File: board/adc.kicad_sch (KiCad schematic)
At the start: 17 parts

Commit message: ERC run
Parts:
- gave numbers to parts that had none: 17
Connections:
- net MCLK: now reaches TP18.1, U4.18 (MCLKIN)
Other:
- moved on the sheet: R17

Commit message: added footprints to symbols and started layout
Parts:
- C22, C23, C24, C25: footprint (none) -> Capacitor_SMD:C_0402_1005Metric
- J10, J11, J12, J13, J14, J7, J8, J9: footprint (none) -> Connector_PinHeader_2.54mm:PinHeader_1x03_P2.54mm_Vertical
- J6: footprint (none) -> Connector_PinHeader_2.54mm:PinHeader_1x02_P2.54mm_Vertical
- R17, R18: footprint (none) -> Resistor_SMD:R_0402_1005Metric
- TP18: footprint (none) -> TestPoint:TestPoint_Pad_D1.0mm
- U4: footprint (none) -> Package_SO:HTSSOP-20-1EP_4.4x6.5mm_P0.65mm_EP3.4x6.5mm_Mask2.75x3.43mm
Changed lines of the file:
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@@
     (property "Reference" "U4" (id 0) (at 120.65 58.42 0))
     (property "Value" "MCP3564RT" (id 1) (at 120.65 60.96 0))
-    (property "Footprint" "" (id 2) (at 109.22 69.85 0)
+    (property "Footprint" "Package_SO:HTSSOP-20-1EP_4.4x6.5mm_P0.65mm_EP3.4x6.5mm_Mask2.75x3.43mm" (id 2) (at 109.22 69.85 0)
       (effects (font (size 1.27 1.27)) hide)
     )
@@
       (effects (font (size 1.27 1.27)) (justify left))
     )
-    (property "Footprint" "" (id 2) (at 99.06 83.82 0)
+    (property "Footprint" "Capacitor_SMD:C_0402_1005Metric" (id 2) (at 99.06 83.82 0)
       (effects (font (size 1.27 1.27)) hide)
     )
@@
       (effects (font (size 1.27 1.27)) (justify left))
     )
-    (property "Footprint" "" (id 2) (at 198.12 25.4 0)
+    (property "Footprint" "Connector_PinHeader_2.54mm:PinHeader_1x03_P2.54mm_Vertical" (id 2) (at 198.12 25.4 0)
       (effects (font (size 1.27 1.27)) hide)
     )
@@
       (effects (font (size 1.27 1.27)) (justify left))
     )
-    (property "Footprint" "" (id 2) (at 86.36 83.82 0)
+    (property "Footprint" "Capacitor_SMD:C_0402_1005Metric" (id 2) (at 86.36 83.82 0)
       (effects (font (size 1.27 1.27)) hide)
     )
@@
       (effects (font (size 1.27 1.27)) (justify left))
     )
-    (property "Footprint" "" (id 2) (at 198.12 152.4 0)
+    (property "Footprint" "Connector_PinHeader_2.54mm:PinHeader_1x03_P2.54mm_Vertical" (id 2) (at 198.12 152.4 0)
       (effects (font (size 1.27 1.27)) hide)
     )
@@
       (effects (font (size 1.27 1.27)) (justify left))
     )
-    (property "Footprint" "" (id 2) (at 198.12 76.2 0)
+    (property "Footprint" "Connector_PinHeader_2.54mm:PinHeader_1x03_P2.54mm_Vertical" (id 2) (at 198.12 76.2 0)
       (effects (font (size 1.27 1.27)) hide)
     )
@@
       (effects (font (size 1.27 1.27)) (justify left))
     )
-    (property "Footprint" "" (id 2) (at 99.06 68.58 0)
+    (property "Footprint" "Capacitor_SMD:C_0402_1005Metric" (id 2) (at 99.06 68.58 0)
       (effects (font (size 1.27 1.27)) hide)
     )
@@
       (effects (font (size 1.27 1.27)) (justify left))
     )
-    (property "Footprint" "" (id 2) (at 198.12 101.6 0)
+    (property "Footprint" "Connector_PinHeader_2.54mm:PinHeader_1x03_P2.54mm_Vertical" (id 2) (at 198.12 101.6 0)
       (effects (font (size 1.27 1.27)) hide)
     )
@@
     (property "Reference" "J6" (id 0) (at 97.79 77.47 0))
     (property "Value" "REF" (id 1) (at 97.79 74.93 0))
-    (property "Footprint" "" (id 2) (at 104.14 77.47 0)
+    (property "Footprint" "Connector_PinHeader_2.54mm:PinHeader_1x02_P2.54mm_Vertical" (id 2) (at 104.14 77.47 0)
       (effects (font (size 1.27 1.27)) hide)
     )
@@
     (property "Reference" "R17" (id 0) (at 69.85 73.66 90))
     (property "Value" "10R" (id 1) (at 69.85 76.2 90))
-    (property "Footprint" "" (id 2) (at 69.85 80.01 0)
+    (property "Footprint" "Resistor_SMD:R_0402_1005Metric" (id 2) (at 69.85 80.01 0)
       (effects (font (size 1.27 1.27)) hide)
     )
@@
       (effects (font (size 1.27 1.27)) (justify left))
     )
-    (property "Footprint" "" (id 2) (at 86.36 68.58 0)
+    (property "Footprint" "Capacitor_SMD:C_0402_1005Metric" (id 2) (at 86.36 68.58 0)
       (effects (font (size 1.27 1.27)) hide)
     )
@@
       (effects (font (size 1.27 1.27)) (justify left))
     )
-    (property "Footprint" "" (id 2) (at 86.36 60.96 0)
+    (property "Footprint" "Resistor_SMD:R_0402_1005Metric" (id 2) (at 86.36 60.96 0)
       (effects (font (size 1.27 1.27)) hide)
     )
@@
       (effects (font (size 1.27 1.27)) (justify right))
     )
-    (property "Footprint" "" (id 2) (at 86.36 97.79 0)
+    (property "Footprint" "TestPoint:TestPoint_Pad_D1.0mm" (id 2) (at 86.36 97.79 0)
       (effects (font (size 1.27 1.27)) hide)
     )
@@
       (effects (font (size 1.27 1.27)) (justify left))
     )
-    (property "Footprint" "" (id 2) (at 198.12 50.8 0)
+    (property "Footprint" "Connector_PinHeader_2.54mm:PinHeader_1x03_P2.54mm_Vertical" (id 2) (at 198.12 50.8 0)
       (effects (font (size 1.27 1.27)) hide)
     )
@@
       (effects (font (size 1.27 1.27)) (justify left))
     )
-    (property "Footprint" "" (id 2) (at 154.94 179.07 0)
+    (property "Footprint" "Connector_PinHeader_2.54mm:PinHeader_1x03_P2.54mm_Vertical" (id 2) (at 154.94 179.07 0)
       (effects (font (size 1.27 1.27)) hide)
     )
@@
       (effects (font (size 1.27 1.27)) (justify left))
     )
-    (property "Footprint" "" (id 2) (at 154.94 153.67 0)
+    (property "Footprint" "Connector_PinHeader_2.54mm:PinHeader_1x03_P2.54mm_Vertical" (id 2) (at 154.94 153.67 0)
       (effects (font (size 1.27 1.27)) hide)
     )
@@
       (effects (font (size 1.27 1.27)) (justify left))
     )
-    (property "Footprint" "" (id 2) (at 198.12 127 0)
-      (effects (font (size 1.27 1.27)) hide)
-    )
+    (property "Footprint" "Connector_PinHeader_2.54mm:PinHeader_1x03_P2.54mm_Vertical" (id 2) (at 198.12 127 0)
+      (effects (font (size 1.27 1.27)) hide)
+    )

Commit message: WIP pushed for meeting
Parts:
- removed TP18: MCLKIN, TestPoint:TestPoint_Pad_D1.0mm, symbol Connector:TestPoint
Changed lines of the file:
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@@
-    (stroke (width 0) (type default) (color 0 0 0 0))
-  )
-  (wire (pts (xy 91.44 93.98) (xy 91.44 97.79))
     (stroke (width 0) (type default) (color 0 0 0 0))
   )
@@
     (effects (font (size 1.27 1.27)) (justify right))
   )
-  (hierarchical_label "MCLK" (shape input) (at 91.44 96.52 180)
+  (hierarchical_label "MCLK" (shape input) (at 91.44 93.98 270)
     (effects (font (size 1.27 1.27)) (justify right))
   )
@@
       (effects (font (size 1.27 1.27)) hide)
     )
-    (pin "1")
-  )
-  (symbol (lib_id "Connector:TestPoint") (at 91.44 97.79 180) (unit 1)
-    (in_bom yes) (on_board yes) (fields_autoplaced)
-    (property "Reference" "TP18" (id 0) (at 93.98 99.8219 0)
-      (effects (font (size 1.27 1.27)) (justify right))
-    )
-    (property "Value" "MCLKIN" (id 1) (at 93.98 102.3619 0)
-      (effects (font (size 1.27 1.27)) (justify right))
-    )
-    (property "Footprint" "TestPoint:TestPoint_Pad_D1.0mm" (id 2) (at 86.36 97.79 0)
-      (effects (font (size 1.27 1.27)) hide)
-    )
-    (property "Datasheet" "~" (id 3) (at 86.36 97.79 0)
-      (effects (font (size 1.27 1.27)) hide)
-    )

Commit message: finished layout for review
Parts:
- U4: footprint Package_SO:HTSSOP-20-1EP_4.4x6.5mm_P0.65mm_EP3.4x6.5mm_Mask2.75x3.43mm -> ownLib:HTSSOP-20-1EP_4.4x6.5mm_P0.65mm_3.4x6.5mm_Mask2.75x3.43mm
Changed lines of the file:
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@@
     (property "Reference" "U4" (id 0) (at 120.65 58.42 0))
     (property "Value" "MCP3564RT" (id 1) (at 120.65 60.96 0))
-    (property "Footprint" "Package_SO:HTSSOP-20-1EP_4.4x6.5mm_P0.65mm_EP3.4x6.5mm_Mask2.75x3.43mm" (id 2) (at 109.22 69.85 0)
+    (property "Footprint" "ownLib:HTSSOP-20-1EP_4.4x6.5mm_P0.65mm_3.4x6.5mm_Mask2.75x3.43mm" (id 2) (at 109.22 69.85 0)
       (effects (font (size 1.27 1.27)) hide)
     )

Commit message: did some minor stuff
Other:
- company: (none) -> Hochschule Pforzheim
- title: (none) -> eduSignal
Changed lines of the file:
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@@
 (kicad_sch (version 20211123) (generator eeschema)
   (paper "A4")
+  (title_block
+    (title "eduSignal")
+    (date "2022-07-14")
+    (rev "1")
+    (company "Hochschule Pforzheim")
+    (comment 1 "Patrick Hanner")
+    (comment 2 "Biosignal development board")
+  )
   (junction (at 86.36 64.77) (diameter 0) (color 0 0 0 0)
   )

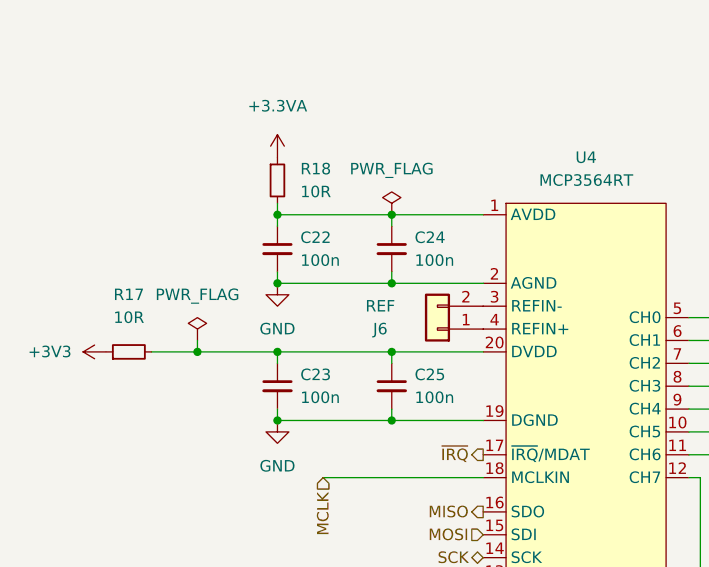
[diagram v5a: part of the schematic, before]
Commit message: fixed errors in schematic
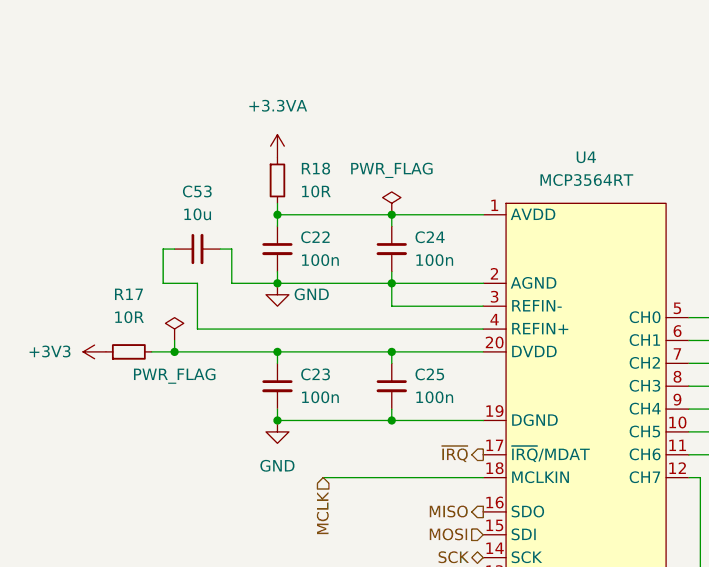
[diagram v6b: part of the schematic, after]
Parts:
- removed J6: REF, Connector_PinHeader_2.54mm:PinHeader_1x02_P2.54mm_Vertical, symbol Connector_Generic:Conn_01x02
- added C53: 10u, Capacitor_SMD:C_0603_1608Metric, symbol Device:C_Small
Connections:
- net GND: now also U4.3 (REFIN-), C53.2
- net at U4.4 (REFIN+): now also C53.1
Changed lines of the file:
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@@
   (junction (at 86.36 87.63) (diameter 0) (color 0 0 0 0)
   )
-  (junction (at 77.47 80.01) (diameter 0) (color 0 0 0 0)
-  )
   (junction (at 99.06 87.63) (diameter 0) (color 0 0 0 0)
   )
+  (junction (at 74.93 80.01) (diameter 0) (color 0 0 0 0)
+  )
   (wire (pts (xy 132.08 86.36) (xy 173.99 86.36))
     (stroke (width 0) (type default) (color 0 0 0 0))
@@
     (stroke (width 0) (type default) (color 0 0 0 0))
   )
-  (wire (pts (xy 77.47 78.74) (xy 77.47 80.01))
+  (wire (pts (xy 73.66 72.39) (xy 73.66 68.58))
+    (stroke (width 0) (type default) (color 0 0 0 0))
+  )
+  (wire (pts (xy 74.93 78.74) (xy 74.93 80.01))
     (stroke (width 0) (type default) (color 0 0 0 0))
   )
@@
     (stroke (width 0) (type default) (color 0 0 0 0))
   )
+  (wire (pts (xy 109.22 77.47) (xy 77.47 77.47))
+    (stroke (width 0) (type default) (color 0 0 0 0))
+  )
   (wire (pts (xy 109.22 93.98) (xy 91.44 93.98))
     (stroke (width 0) (type default) (color 0 0 0 0))
@@
     (stroke (width 0) (type default) (color 0 0 0 0))
   )
+  (wire (pts (xy 73.66 68.58) (xy 74.93 68.58))
+    (stroke (width 0) (type default) (color 0 0 0 0))
+  )
   (wire (pts (xy 99.06 86.36) (xy 99.06 87.63))
     (stroke (width 0) (type default) (color 0 0 0 0))
@@
     (stroke (width 0) (type default) (color 0 0 0 0))
   )
+  (wire (pts (xy 81.28 68.58) (xy 81.28 72.39))
+    (stroke (width 0) (type default) (color 0 0 0 0))
+  )
   (wire (pts (xy 191.77 72.39) (xy 191.77 73.66))
     (stroke (width 0) (type default) (color 0 0 0 0))
@@
     (stroke (width 0) (type default) (color 0 0 0 0))
   )
+  (wire (pts (xy 81.28 72.39) (xy 86.36 72.39))
+    (stroke (width 0) (type default) (color 0 0 0 0))
+  )
   (wire (pts (xy 173.99 50.8) (xy 193.04 50.8))
     (stroke (width 0) (type default) (color 0 0 0 0))
@@
     (stroke (width 0) (type default) (color 0 0 0 0))
   )
+  (wire (pts (xy 109.22 74.93) (xy 99.06 74.93))
+    (stroke (width 0) (type default) (color 0 0 0 0))
+  )
   (wire (pts (xy 149.86 181.61) (xy 148.59 181.61))
     (stroke (width 0) (type default) (color 0 0 0 0))
@@
     (stroke (width 0) (type default) (color 0 0 0 0))
   )
+  (wire (pts (xy 99.06 74.93) (xy 99.06 72.39))
+    (stroke (width 0) (type default) (color 0 0 0 0))
+  )
   (wire (pts (xy 193.04 78.74) (xy 191.77 78.74))
     (stroke (width 0) (type default) (color 0 0 0 0))
@@
     (stroke (width 0) (type default) (color 0 0 0 0))
   )
-  (wire (pts (xy 77.47 80.01) (xy 86.36 80.01))
+  (wire (pts (xy 74.93 80.01) (xy 86.36 80.01))
     (stroke (width 0) (type default) (color 0 0 0 0))
   )
@@
     (stroke (width 0) (type default) (color 0 0 0 0))
   )
+  (wire (pts (xy 80.01 68.58) (xy 81.28 68.58))
+    (stroke (width 0) (type default) (color 0 0 0 0))
+  )
   (wire (pts (xy 171.45 76.2) (xy 171.45 25.4))
     (stroke (width 0) (type default) (color 0 0 0 0))
@@
     (stroke (width 0) (type default) (color 0 0 0 0))
   )
+  (wire (pts (xy 72.39 80.01) (xy 74.93 80.01))
+    (stroke (width 0) (type default) (color 0 0 0 0))
+  )
   (wire (pts (xy 191.77 22.86) (xy 193.04 22.86))
     (stroke (width 0) (type default) (color 0 0 0 0))
@@
     (stroke (width 0) (type default) (color 0 0 0 0))
   )
+  (wire (pts (xy 77.47 72.39) (xy 73.66 72.39))
+    (stroke (width 0) (type default) (color 0 0 0 0))
+  )
   (wire (pts (xy 193.04 53.34) (xy 191.77 53.34))
     (stroke (width 0) (type default) (color 0 0 0 0))
@@
     (stroke (width 0) (type default) (color 0 0 0 0))
   )
-  (wire (pts (xy 72.39 80.01) (xy 77.47 80.01))
-    (stroke (width 0) (type default) (color 0 0 0 0))
-  )
   (wire (pts (xy 191.77 97.79) (xy 191.77 99.06))
     (stroke (width 0) (type default) (color 0 0 0 0))
@@
   )
   (wire (pts (xy 135.89 91.44) (xy 135.89 153.67))
+    (stroke (width 0) (type default) (color 0 0 0 0))
+  )
+  (wire (pts (xy 77.47 77.47) (xy 77.47 72.39))
     (stroke (width 0) (type default) (color 0 0 0 0))
   )
@@
     (pin "1")
   )
-  (symbol (lib_id "power:PWR_FLAG") (at 77.47 78.74 0) (unit 1)
-    (in_bom yes) (on_board yes) (fields_autoplaced)
-    (property "Reference" "#FLG0106" (id 0) (at 77.47 76.835 0)
-      (effects (font (size 1.27 1.27)) hide)
-    )
-    (property "Value" "PWR_FLAG" (id 1) (at 77.47 73.66 0))
-    (property "Footprint" "" (id 2) (at 77.47 78.74 0)
-      (effects (font (size 1.27 1.27)) hide)
-    )
-    (property "Datasheet" "~" (id 3) (at 77.47 78.74 0)
+  (symbol (lib_id "power:PWR_FLAG") (at 74.93 78.74 0) (unit 1)
+    (in_bom yes) (on_board yes)
+    (property "Reference" "#FLG0106" (id 0) (at 74.93 76.835 0)
+      (effects (font (size 1.27 1.27)) hide)
+    )
+    (property "Value" "PWR_FLAG" (id 1) (at 74.93 82.55 0))
+    (property "Footprint" "" (id 2) (at 74.93 78.74 0)
+      (effects (font (size 1.27 1.27)) hide)
+    )
+    (property "Datasheet" "~" (id 3) (at 74.93 78.74 0)
       (effects (font (size 1.27 1.27)) hide)
     )
@@
     (pin "1")
   )
+  (symbol (lib_id "Device:C_Small") (at 77.47 68.58 90) (unit 1)
+    (in_bom yes) (on_board yes) (fields_autoplaced)
+    (property "Reference" "C53" (id 0) (at 77.4763 62.23 90))
+    (property "Value" "10u" (id 1) (at 77.4763 64.77 90))
+    (property "Footprint" "Capacitor_SMD:C_0603_1608Metric" (id 2) (at 77.47 68.58 0)
+      (effects (font (size 1.27 1.27)) hide)
+    )
+    (property "Datasheet" "~" (id 3) (at 77.47 68.58 0)
+      (effects (font (size 1.27 1.27)) hide)
+    )
+    (pin "1")
+    (pin "2")
+  )
   (symbol (lib_id "power:GND") (at 191.77 54.61 0) (unit 1)
     (in_bom yes) (on_board yes) (fields_autoplaced)
@@
     (pin "2")
     (pin "3")
-  )
-  (symbol (lib_id "Connector_Generic:Conn_01x02") (at 104.14 77.47 180) (unit 1)
-    (in_bom yes) (on_board yes)
-    (property "Reference" "J6" (id 0) (at 97.79 77.47 0))
-    (property "Value" "REF" (id 1) (at 97.79 74.93 0))
-    (property "Footprint" "Connector_PinHeader_2.54mm:PinHeader_1x02_P2.54mm_Vertical" (id 2) (at 104.14 77.47 0)
-      (effects (font (size 1.27 1.27)) hide)
-    )
-    (property "Datasheet" "~" (id 3) (at 104.14 77.47 0)
-      (effects (font (size 1.27 1.27)) hide)
-    )
-    (pin "1")
-    (pin "2")
   )
   (symbol (lib_id "Device:R_Small") (at 69.85 80.01 90) (unit 1)
@@
   )
   (symbol (lib_id "power:GND") (at 86.36 72.39 0) (unit 1)
-    (in_bom yes) (on_board yes) (fields_autoplaced)
+    (in_bom yes) (on_board yes)
     (property "Reference" "#PWR022" (id 0) (at 86.36 78.74 0)
       (effects (font (size 1.27 1.27)) hide)
     )
-    (property "Value" "GND" (id 1) (at 86.36 77.47 0))
+    (property "Value" "GND" (id 1) (at 90.17 73.66 0))
     (property "Footprint" "" (id 2) (at 86.36 72.39 0)
       (effects (font (size 1.27 1.27)) hide)
